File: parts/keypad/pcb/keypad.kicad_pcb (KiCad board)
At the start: 2 copper layers, 95 x 74.5 mm, 22 parts, among them J1 Conn_02x10_Top_Bottom, J2 1x10, J3 To MCU, J4 To DISP, SW1 SW_Push, SW10 SW_Push, SW2 SW_Push, SW3 SW_Push, SW4 SW_Push, SW5 SW_Push, SW6 SW_Push, SW7 SW_Push, SW8 SW_Push, SW9 SW_Push

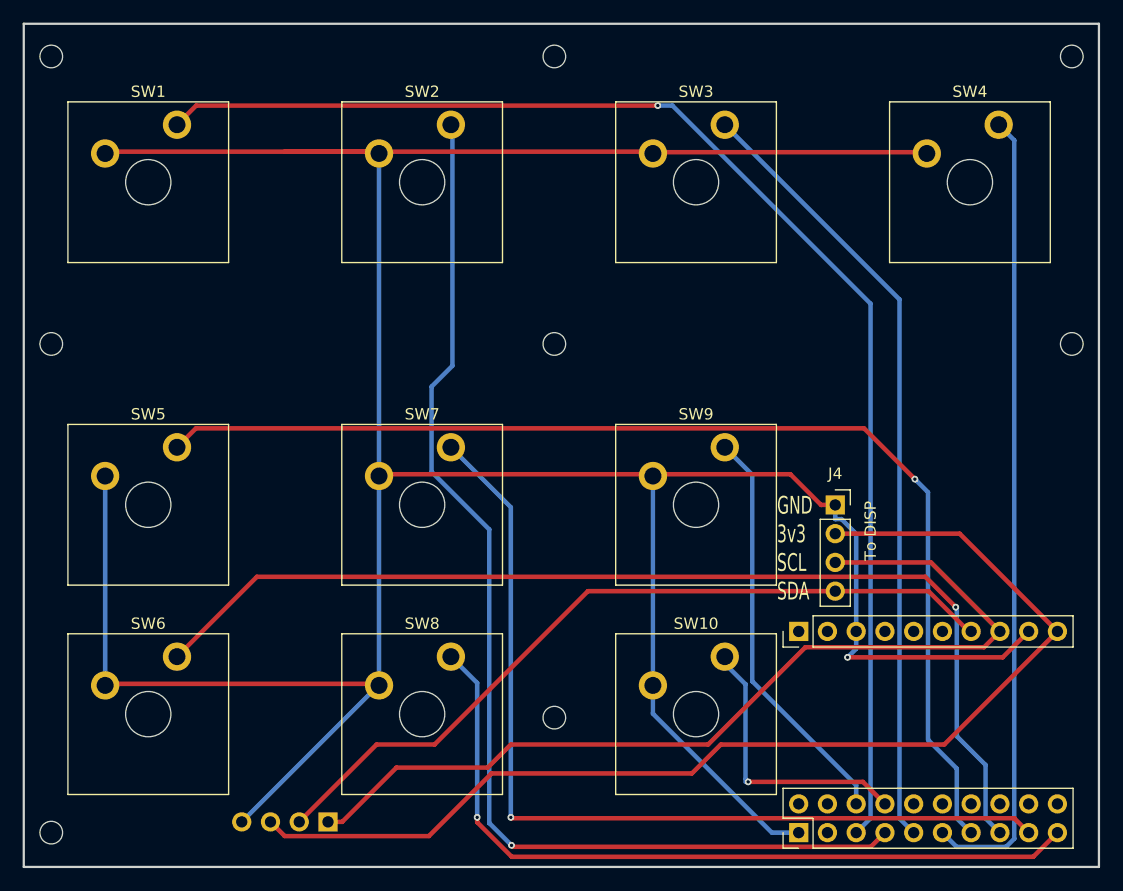
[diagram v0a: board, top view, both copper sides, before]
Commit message: revise keypad due to soldering screw up (now rev 1.6); add todo notes.
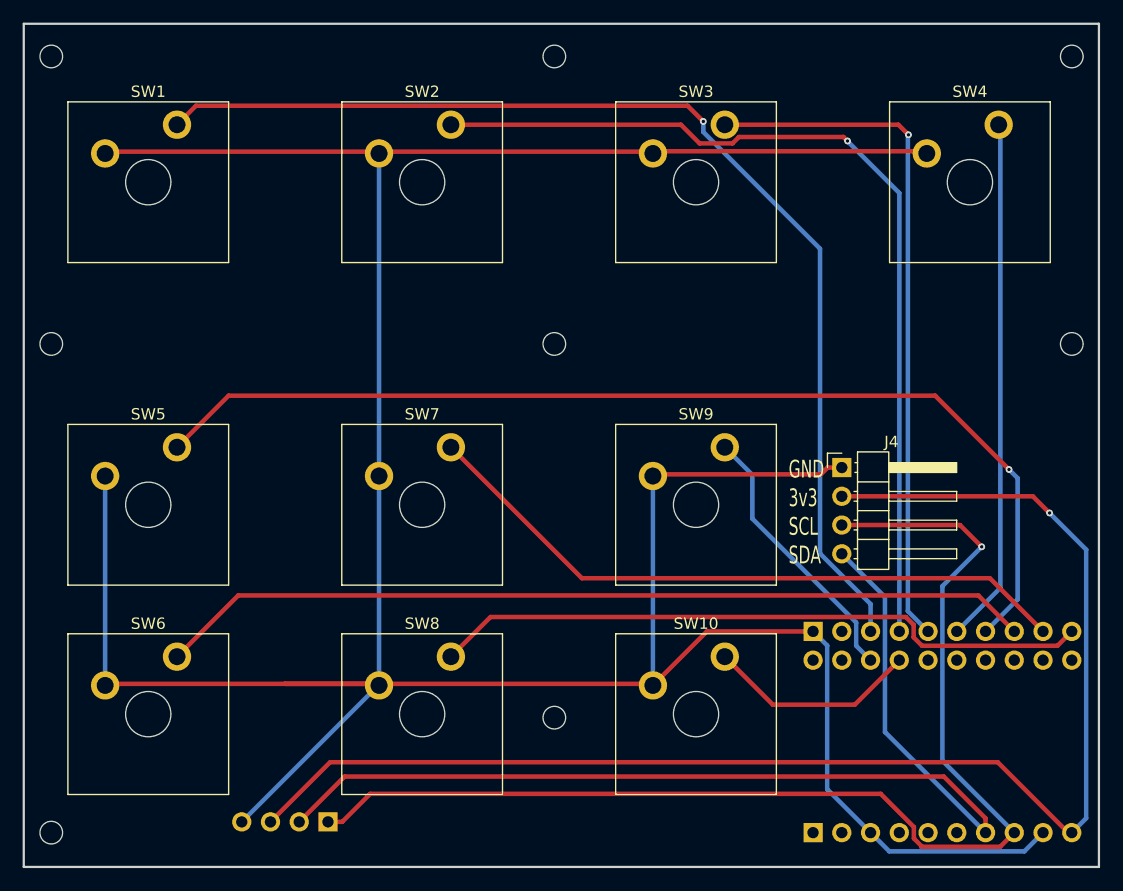
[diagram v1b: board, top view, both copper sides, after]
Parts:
- J1, J2: moved to B.Cu
- J3: value To MCU -> To SENSOR HUB
- J4: value To DISP -> To DISPLAY MODULE; footprint Connector_PinSocket_2.54mm:PinSocket_1x04_P2.54mm_Vertical -> Connector_PinHeader_2.54mm:PinHeader_1x04_P2.54mm_Horizontal
- moved J1 17.8 mm to (98.7, 79.7), turned to -90 degrees
- moved J2 17.8 mm to (98.7, 97.5), turned to -90 degrees
- moved J4 3.35 mm to (101.3, 65.2)
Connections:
- net /COM renamed /GND
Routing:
- net Net-(J2-SDA): track 69.1 -> 95.0 mm
- net /N$4: track 70.8 -> 46.2 mm
- net Net-(J2-SCL): track 83.4 -> 107.3 mm, vias 0 -> 1
- net Net-(J2-3V3): track 100.7 -> 124.3 mm, vias 0 -> 1
- net /N$7: track 81.2 -> 59.1 mm, vias 1 -> 0
- net /N$2: track 100.8 -> 81.3 mm
- net /N$1: track 116.5 -> 99.0 mm
- net /N$6: track 94.4 -> 77.5 mm, vias 1 -> 0
- net /N$9: track 36.3 -> 24.1 mm
- net /N$8: track 69.0 -> 58.5 mm, vias 1 -> 0
- net /N$3: track 69.5 -> 61.2 mm, vias 0 -> 1
- net /N$5: track 101.0 -> 93.9 mm
- net /N$10: track 24.4 -> 18.8 mm, vias 1 -> 0
- net /GND: track 297.7 -> 298.3 mm, vias 1 -> 0
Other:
- board text added: "(C) 2026 ARKADIA HOUSE Keypad Display rev 01.6"
- board text added: "MCP23017 module"
- board text removed: "(C) 2026 ARKADIA HOUSE Keypad Display rev 01.5.2"
- board text removed: "MCP23017 module topside down"
- board text removed: "V/GND ITB/ITA B0/A0 B1/A1 B2/A2 B3/A3 B4/A4 B5/A5 B6/A6 B7/A7"
